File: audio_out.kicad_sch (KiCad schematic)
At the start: 32 parts, among them U3 PAM8908JER, U4 PCM5102A, U8 AP7333-33SRG-7

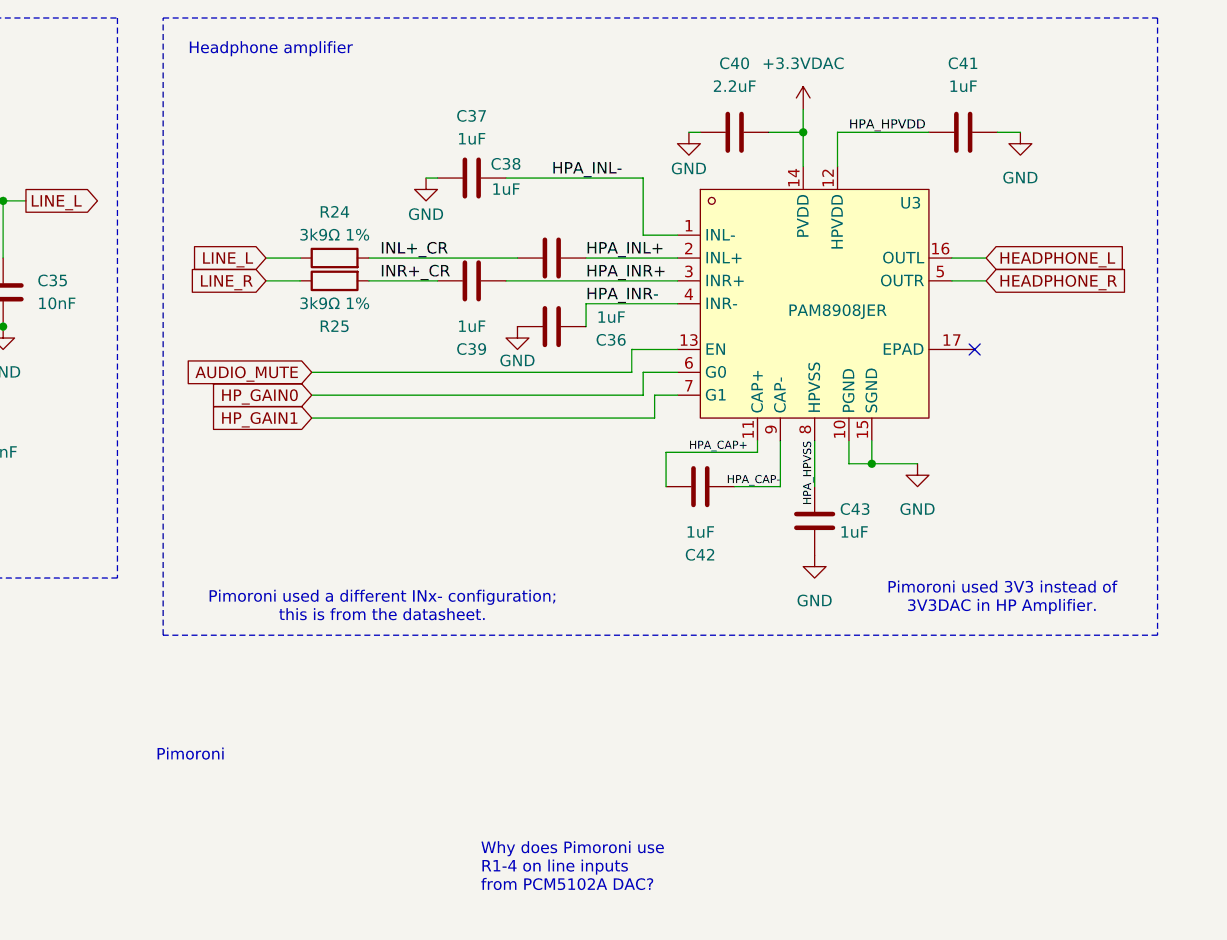
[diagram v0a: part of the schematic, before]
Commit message: Add female jumper to allow experimenting with Pimoroni circuit (default 1kΩ). Minor cleanups.
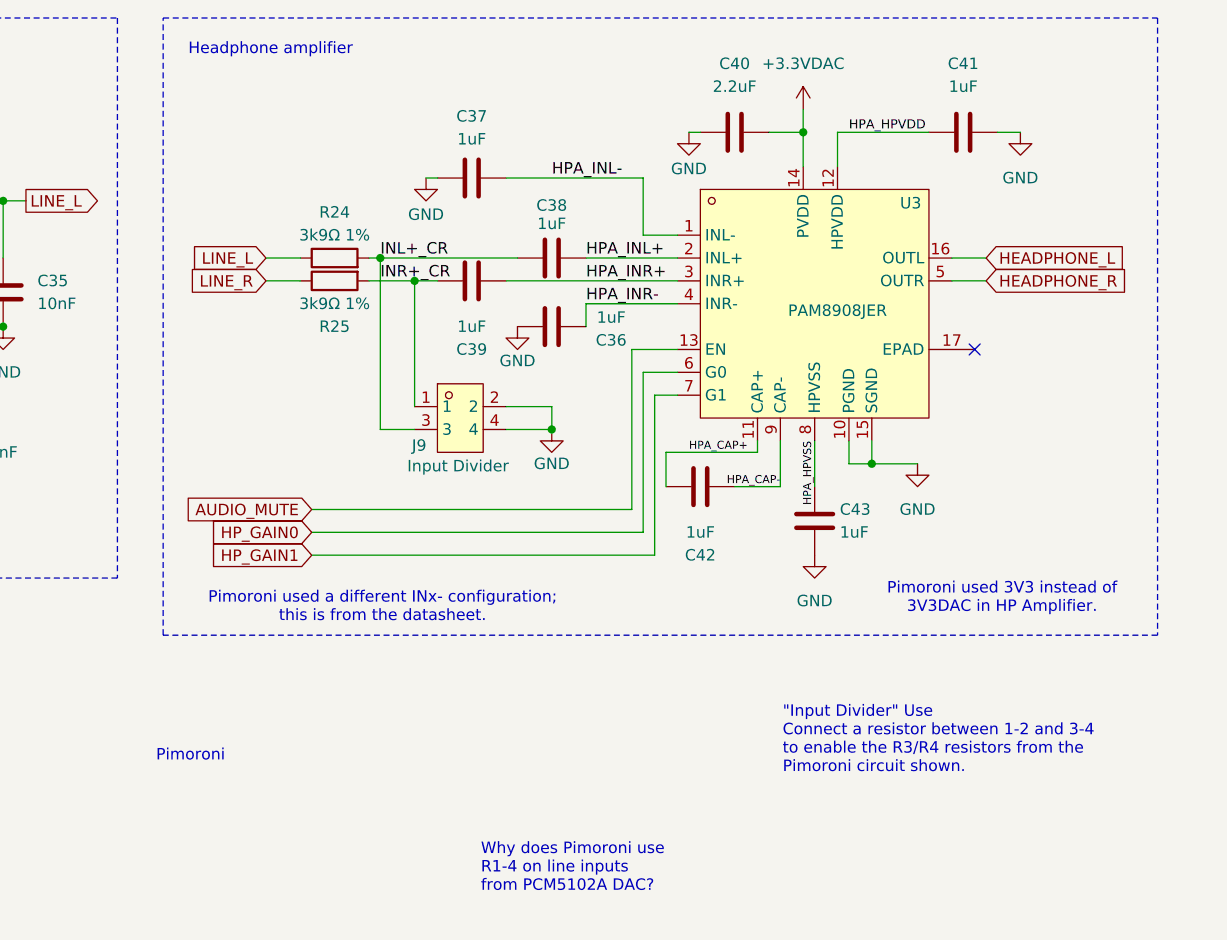
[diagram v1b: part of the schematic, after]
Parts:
- added J9: Input Divider, easyeda2kicad:HDR-TH_4P-P2.54-V-F-R2-C2-S2.54, symbol easyeda2kicad:排母_2.54MM2X2直排母袋装环保
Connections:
- net INR+_CR is gone; now on net INL+_CR: C39.1, R25.2
- net GND: now also J9.2, J9.4
- net INL+_CR: now also J9.1, J9.3
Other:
- note added: ""Input Divider" Use Connect a resistor between 1-2 and 3-4 to enable the R3/R4 resistors from the Pimoroni circuit shown."

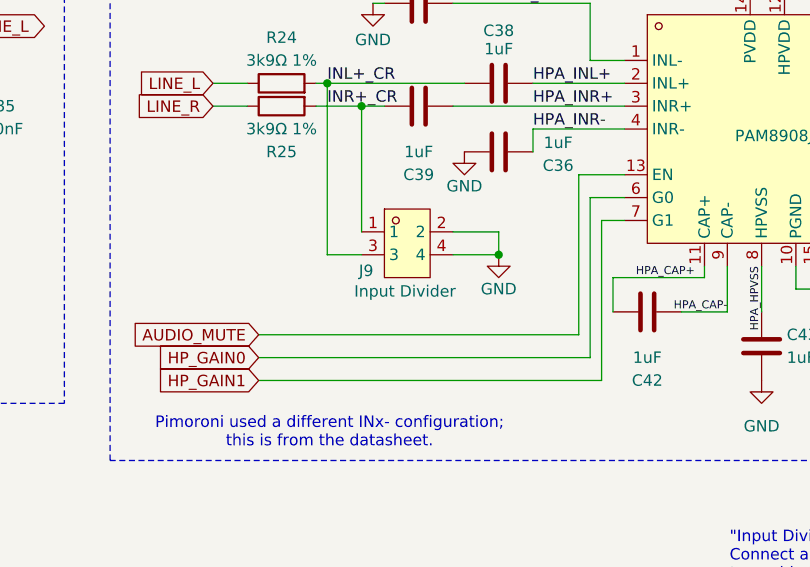
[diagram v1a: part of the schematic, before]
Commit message: Prepare EVT2 for JLCPCB by replacing parts not in stock and generating necessary outputs.
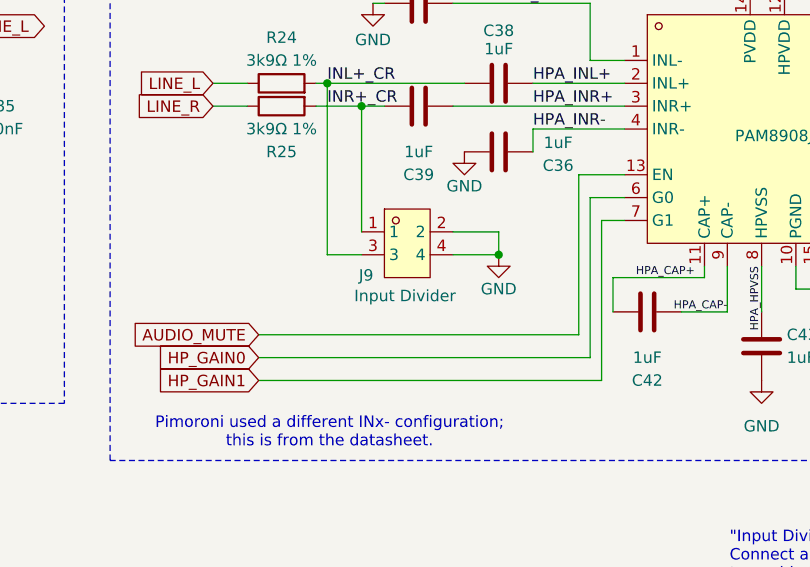
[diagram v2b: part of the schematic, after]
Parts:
- removed J9: Input Divider, easyeda2kicad:HDR-TH_4P-P2.54-V-F-R2-C2-S2.54, symbol easyeda2kicad:排母_2.54MM2X2直排母袋装环保
- added J9: Input Divider, easyeda2kicad:HDR-TH_4P-P2.54-V-F-R2-C2-S2.54, symbol easyeda2kicad:2.54-2*2
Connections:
- net GND: now also J9.2, J9.4
- net INL+_CR: now also J9.1, J9.3
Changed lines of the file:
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@@
 	)
 	(symbol
-		(lib_id "easyeda2kicad:排母_2.54MM2X2直排母袋装环保")
-		(at 173.99 62.23 0)
-		(unit 1)
-		(exclude_from_sim no)
-		(in_bom yes)
-		(on_board yes)
-		(dnp no)
-		(property "Reference" "J9"
-			(at 169.418 65.278 0)
-			(effects
-				(font
-					(size 1.27 1.27)
-				)
-			)
-		)
-		(property "Value" "Input Divider"
-			(at 173.736 67.564 0)
-			(effects
-				(font
-					(size 1.27 1.27)
-				)
-			)
-		)
-		(property "Footprint" "easyeda2kicad:HDR-TH_4P-P2.54-V-F-R2-C2-S2.54"
-			(at 173.99 71.12 0)
-			(effects
-				(font
-					(size 1.27 1.27)
-				)
-				(hide yes)
-			)
-		)
-		(property "Datasheet" ""
-			(at 173.99 62.23 0)
-			(effects
-				(font
-					(size 1.27 1.27)
-				)
-				(hide yes)
-			)
-		)
-		(property "Description" ""
-			(at 173.99 62.23 0)
-			(effects
-				(font
-					(size 1.27 1.27)
-				)
-				(hide yes)
-			)
-		)
-		(property "LCSC Part" "C47553"
-			(at 173.99 73.66 0)
-			(effects
-				(font
-					(size 1.27 1.27)
-				)
-				(hide yes)
-			)
-		)
-		(pin "4"
-		)
-		(pin "3"
-		)
-		(pin "1"
-		)
-		(pin "2"
-		)
-		(instances
-			(project ""
-				(path "/7cd74113-1f92-4dcc-8610-19aa9fc81e5f/c9577070-7433-48cd-ae0f-c607bda27147"
-					(reference "J9")
-					(unit 1)
-				)
-			)
-		)
-	)
-	(symbol
 		(lib_id "Device:C")
 		(at 175.26 46.99 90)
@@
 					(unit 1)
 				)
+			)
+		)
+	)
+	(symbol
+		(lib_id "easyeda2kicad:2.54-2*2")
+		(at 173.99 62.23 0)
+		(unit 1)
+		(exclude_from_sim no)
+		(in_bom yes)
+		(on_board yes)
+		(dnp no)
+		(property "Reference" "J9"
+			(at 169.418 65.786 0)
+			(effects
+				(font
+					(size 1.27 1.27)
+				)
+			)
+		)
+		(property "Value" "Input Divider"
+			(at 173.736 68.072 0)
+			(effects
+				(font
+					(size 1.27 1.27)
+				)
+			)
+		)
+		(property "Footprint" "easyeda2kicad:HDR-TH_4P-P2.54-V-F-R2-C2-S2.54"
+			(at 173.99 71.12 0)
+			(effects
+				(font
+					(size 1.27 1.27)
+				)
+				(hide yes)
+			)
+		)
+		(property "Datasheet" ""
+			(at 173.99 62.23 0)
+			(effects
+				(font
+					(size 1.27 1.27)
+				)
+				(hide yes)
+			)
+		)
+		(property "Description" ""
+			(at 173.99 62.23 0)
+			(effects
+				(font
+					(size 1.27 1.27)
+				)
+				(hide yes)
+			)
+		)
+		(property "LCSC Part" "C2977590"
+			(at 173.99 73.66 0)
+			(effects
+				(font
+					(size 1.27 1.27)
+				)
+				(hide yes)
+			)
+		)
+		(pin "2"
+		)
+		(pin "4"
+		)
+		(pin "3"
+		)
+		(pin "1"
+		)
+		(instances
+			(project ""
+				(path "/7cd74113-1f92-4dcc-8610-19aa9fc81e5f/c9577070-7433-48cd-ae0f-c607bda27147"
+					(reference "J9")
+					(unit 1)
+				)

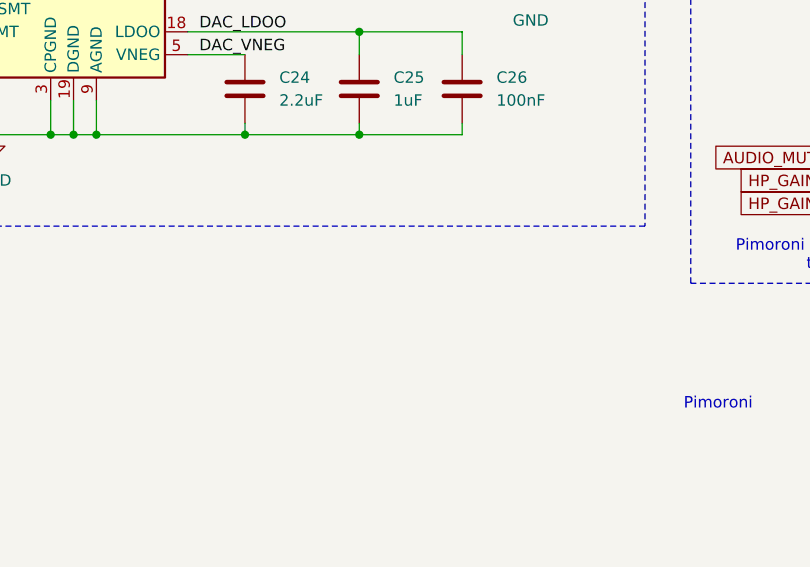
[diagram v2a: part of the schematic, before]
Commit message: Received EVT #2 boards. Testing so far reveals no problems.
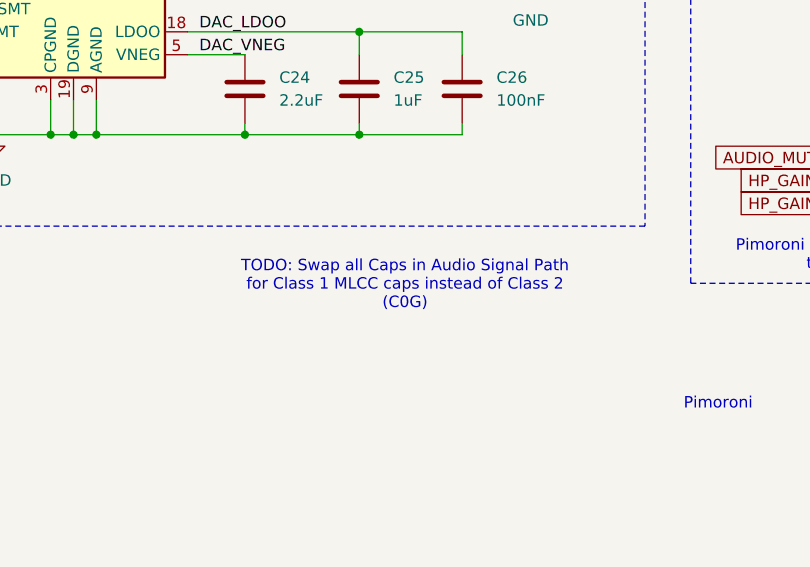
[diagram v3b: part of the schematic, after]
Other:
- note added: "TODO: Swap all Caps in Audio Signal Path for Class 1 MLCC caps instead of Class 2 (C0G)"
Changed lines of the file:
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@@
+		)
+	)
+	(text "TODO: Swap all Caps in Audio Signal Path\nfor Class 1 MLCC caps instead of Class 2\n(C0G)"
+		(exclude_from_sim no)
+		(at 109.22 86.614 0)
+		(effects
+			(font
+				(size 1.27 1.27)
+			)
 		)
 	)
